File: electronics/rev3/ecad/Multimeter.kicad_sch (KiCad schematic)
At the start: 20 parts, among them J1 USB_B, SW1 GF-123-0054, U1 RP2040, U5 LM1117MP-3.3, Y1 ABLS-12.000MHZ-B4-T

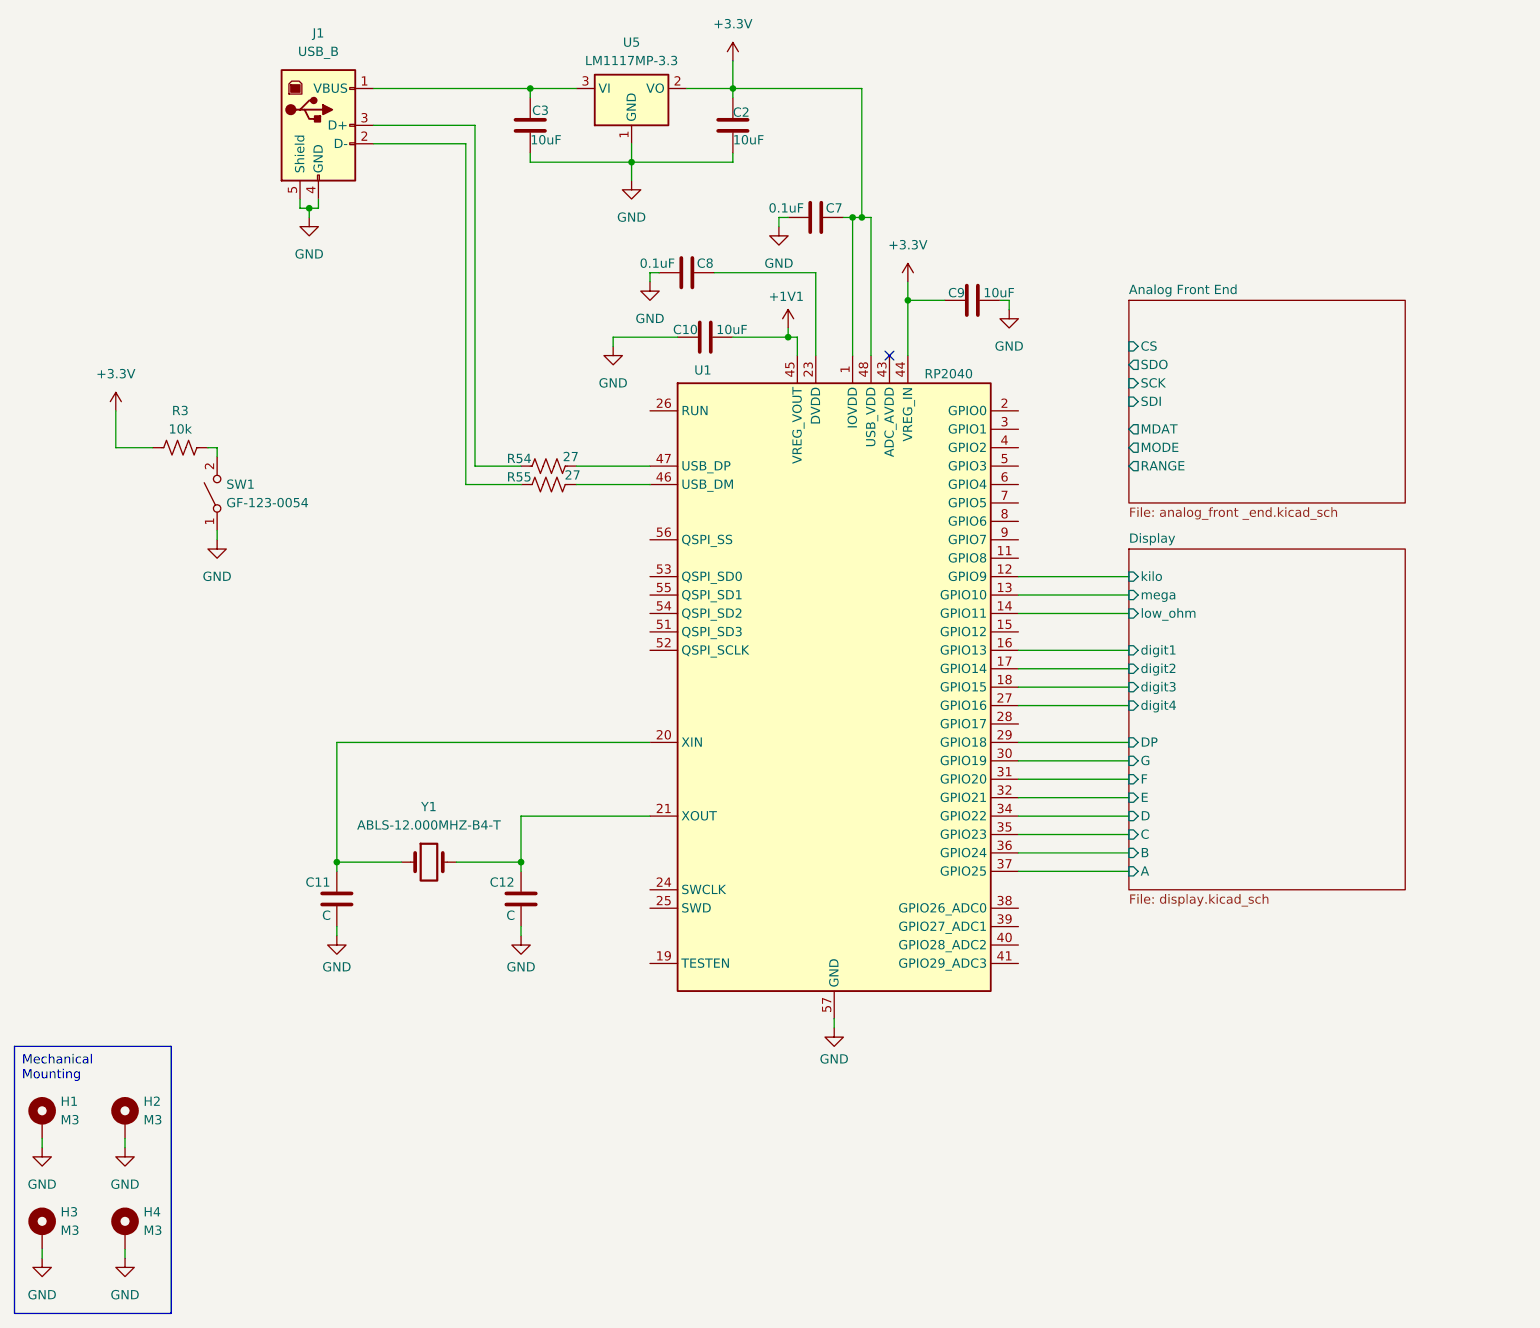
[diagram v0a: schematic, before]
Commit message: rev3 schematic work
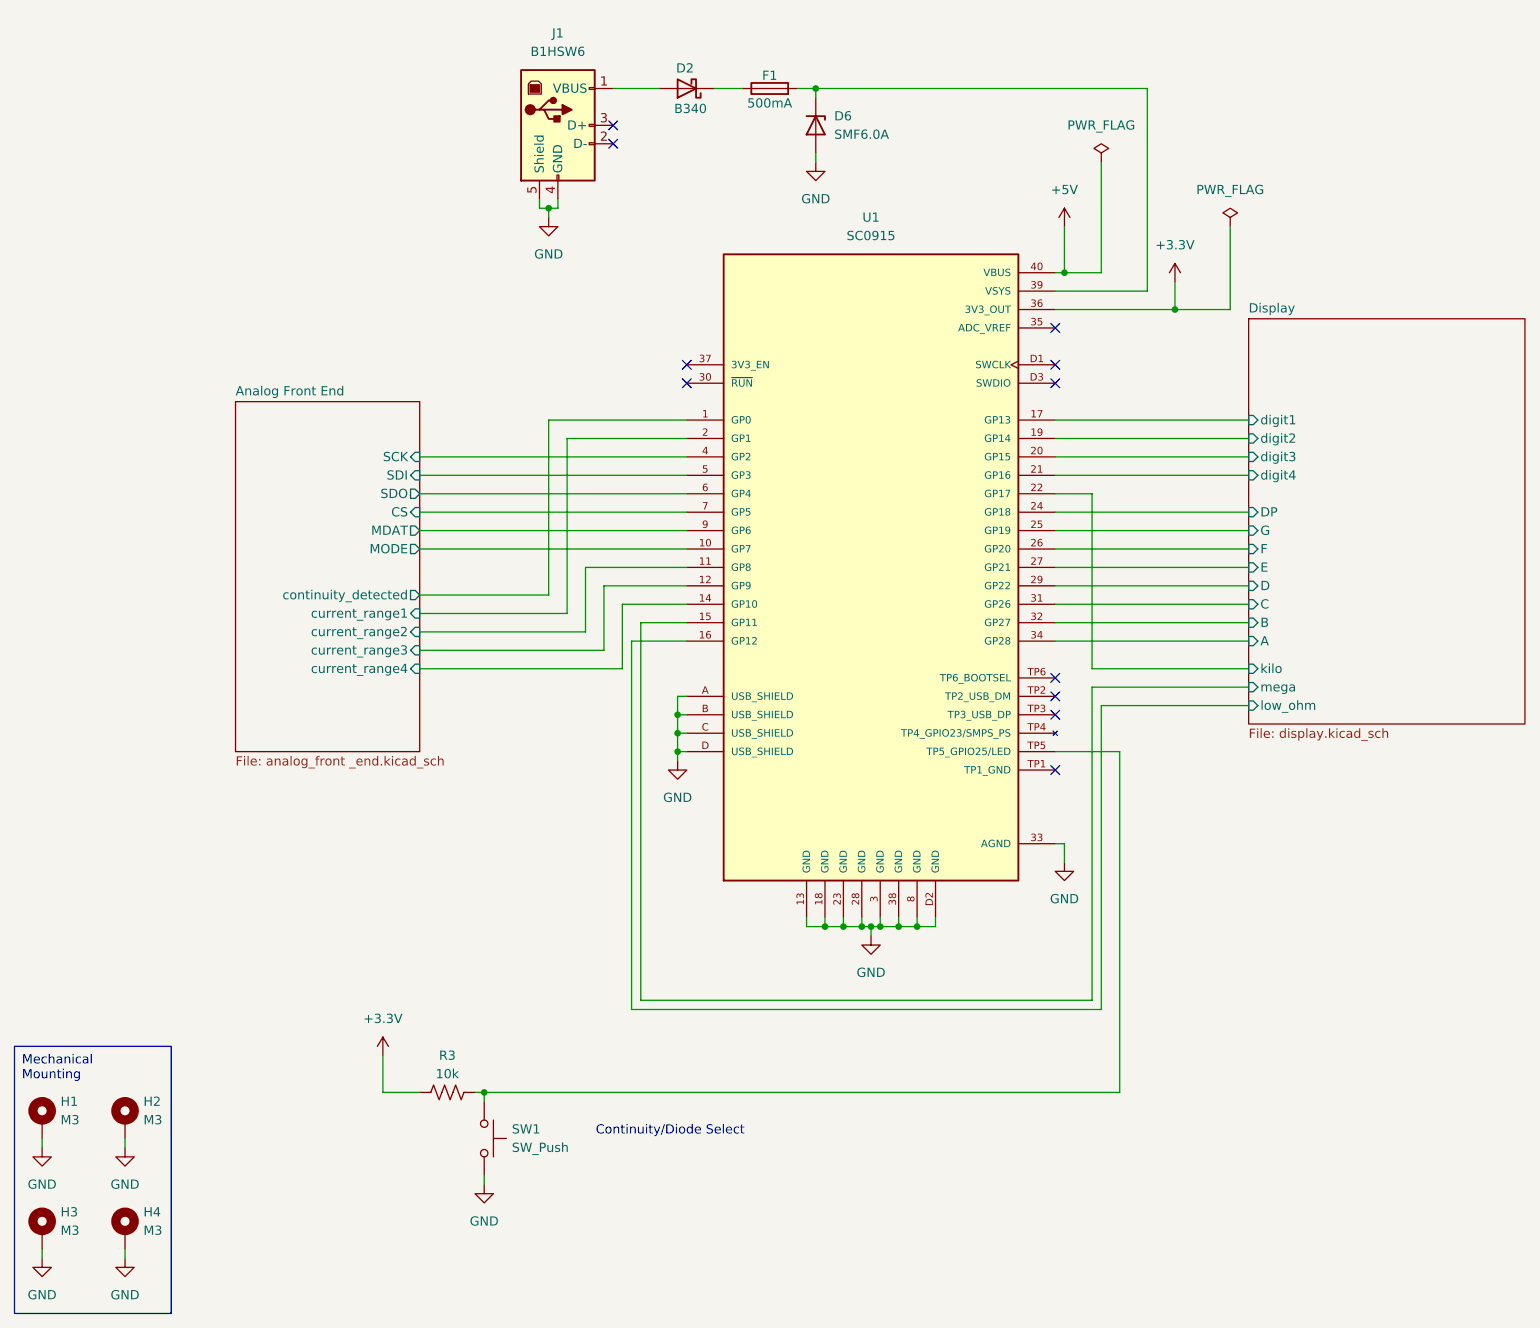
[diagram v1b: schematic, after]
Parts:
- removed C10, C2, C3, C9: 10uF, symbol Device:C
- removed C11, C12: C, symbol Device:C
- removed C7, C8: 0.1uF, symbol Device:C
- removed R54, R55: 27, symbol Device:R_US
- removed SW1: GF-123-0054, Multimeter:SW_GF-123-0054, symbol Switch:SW_SPST
- removed U1: RP2040, Package_DFN_QFN:QFN-56-1EP_7x7mm_P0.4mm_EP3.2x3.2mm, symbol MCU_RaspberryPi:RP2040
- removed U5: LM1117MP-3.3, Package_TO_SOT_SMD:SOT-223-3_TabPin2, symbol Regulator_Linear:LM1117MP-3.3
- removed Y1: ABLS-12.000MHZ-B4-T, symbol Device:Crystal
- added D2: B340, symbol Device:D_Schottky
- added D6: SMF6.0A, symbol Device:D_Zener
- added F1: 500mA, Fuse:Fuse_0805_2012Metric, symbol Device:Fuse
- added SW1: SW_Push, symbol Switch:SW_Push
- added U1: SC0915, SC0915:MODULE_SC0915, symbol multimeter_parts:SC0915
- J1: value USB_B -> B1HSW6
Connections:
- net +3.3V: now also U1.36 (3V3_OUT)
- net Analog Front End/CS: now also U1.7 (GP5)
- net Analog Front End/MDAT: now also U1.9 (GP6)
- net Analog Front End/MODE: now also U1.10 (GP7)
- net Analog Front End/SCK: now also U1.4 (GP2)
- net Analog Front End/SDI: now also U1.5 (GP3)
- net Analog Front End/SDO: now also U1.6 (GP4)
- net Display/A: now also U1.34 (GP28)
- net Display/B: now also U1.32 (GP27)
- net Display/C: now also U1.31 (GP26)
- net Display/D: now also U1.29 (GP22)
- net Display/DP: now also U1.24 (GP18)
- net Display/E: now also U1.27 (GP21)
- net Display/F: now also U1.26 (GP20)
- net Display/G: now also U1.25 (GP19)
- net Display/digit1: now also U1.17 (GP13)
- net Display/digit2: now also U1.19 (GP14)
- net Display/digit3: now also U1.20 (GP15)
- net Display/digit4: now also U1.21 (GP16)
- net Display/kilo: now also U1.22 (GP17)
- net Display/low_ohm: now also U1.16 (GP12)
- net Display/mega: now also U1.15 (GP11)
- net GND: now also D6.2 (A), SW1.2, U1.13 (GND), U1.18 (GND), U1.23 (GND), U1.28 (GND), U1.3 (GND), U1.33 (AGND), U1.38 (GND), U1.8 (GND), U1.A (USB_SHIELD), U1.B (USB_SHIELD), U1.C (USB_SHIELD), U1.D (USB_SHIELD), U1.D2 (GND)
- net at J1.1 (VBUS): now also D2.2 (A)
- net at R3.2: now also SW1.1, U1.TP5 (TP5_GPIO25/LED)
- new net: D2.1 (K), F1.1
- new net: D6.1 (K), F1.2, U1.39 (VSYS)
- new net +5V: U1.40 (VBUS)
- new net Analog Front End/continuity_detected: U1.1 (GP0)
- new net Analog Front End/current_range1: U1.2 (GP1)
- new net Analog Front End/current_range2: U1.11 (GP8)
- new net Analog Front End/current_range3: U1.12 (GP9)
- new net Analog Front End/current_range4: U1.14 (GP10)
- no-connect marks 1 -> 11
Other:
- sheet Analog Front End ports: added continuity_detected, current_range1, current_range2, current_range3, current_range4; removed RANGE
- note added: "Continuity/Diode Select"
- moved on the sheet: J1, R3

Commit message: layout work rev3
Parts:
- D2: footprint (none) -> Diode_SMD:D_SMB
- D6: footprint (none) -> Diode_SMD:D_SOD-123F
- H1, H2, H3, H4: footprint MountingHole:MountingHole_2.7mm_Pad_Via -> MountingHole:MountingHole_3.2mm_M3_Pad_Via
- J1: footprint (none) -> Connector_USB:USB_B_OST_USB-B1HSxx_Horizontal
- R3: footprint Capacitor_SMD:C_0805_2012Metric_Pad1.18x1.45mm_HandSolder -> Resistor_SMD:R_0805_2012Metric
- SW1: footprint (none) -> Button_Switch_THT:SW_PUSH_6mm
- U1: footprint SC0915:MODULE_SC0915 -> Multimeter:MODULE_SC0915
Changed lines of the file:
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@@
+	)
+	(junction
+		(at 148.59 27.94)
+		(diameter 0)
+		(color 0 0 0 0)
 	)
 	(junction
@@
 	(wire
 		(pts
-			(xy 132.08 27.94) (xy 177.8 27.94)
+			(xy 132.08 27.94) (xy 148.59 27.94)
 		)
 		(stroke
@@
 	(wire
 		(pts
+			(xy 148.59 27.94) (xy 177.8 27.94)
+		)
+		(stroke
+			(width 0)
+			(type default)
+		)
+	)
+	(wire
+		(pts
 			(xy 77.47 97.79) (xy 95.25 97.79)
 		)
@@
 		(pts
 			(xy 170.18 107.95) (xy 170.18 83.82)
+		)
+		(stroke
+			(width 0)
+			(type default)
+		)
+	)
+	(wire
+		(pts
+			(xy 148.59 25.4) (xy 148.59 27.94)
 		)
 		(stroke
@@
 			)
 		)
-		(property "Footprint" "MountingHole:MountingHole_2.7mm_Pad_Via"
+		(property "Footprint" "MountingHole:MountingHole_3.2mm_M3_Pad_Via"
 			(at 36.83 170.18 0)
 			(effects
@@
 			)
 		)
-		(property "Footprint" ""
+		(property "Footprint" "Diode_SMD:D_SMB"
 			(at 114.3 27.94 0)
 			(effects
@@
 			)
 		)
-		(property "Footprint" "MountingHole:MountingHole_2.7mm_Pad_Via"
+		(property "Footprint" "MountingHole:MountingHole_3.2mm_M3_Pad_Via"
 			(at 36.83 185.42 0)
 			(effects
@@
 			)
 		)
-		(property "Footprint" ""
+		(property "Footprint" "Diode_SMD:D_SOD-123F"
 			(at 132.08 33.02 0)
 			(effects
@@
 			)
 		)
-		(property "Footprint" "SC0915:MODULE_SC0915"
+		(property "Footprint" "Multimeter:MODULE_SC0915"
 			(at 139.7 93.98 0)
 			(effects
@@
 			)
 		)
-		(property "Footprint" "MountingHole:MountingHole_2.7mm_Pad_Via"
+		(property "Footprint" "MountingHole:MountingHole_3.2mm_M3_Pad_Via"
 			(at 25.4 170.18 0)
 			(effects
@@
 			)
 		)
-		(property "Footprint" ""
+		(property "Footprint" "Button_Switch_THT:SW_PUSH_6mm"
 			(at 91.44 172.72 0)
 			(effects
@@
 			)
 		)
-		(property "Footprint" "MountingHole:MountingHole_2.7mm_Pad_Via"
+		(property "Footprint" "MountingHole:MountingHole_3.2mm_M3_Pad_Via"
 			(at 25.4 185.42 0)
 			(effects
@@
 	)
 	(symbol
+		(lib_id "power:PWR_FLAG")
+		(at 148.59 25.4 0)
+		(unit 1)
+		(exclude_from_sim no)
+		(in_bom yes)
+		(on_board yes)
+		(dnp no)
+		(fields_autoplaced yes)
+		(property "Reference" "#FLG3"
+			(at 148.59 23.495 0)
+			(effects
+				(font
+					(size 1.27 1.27)
+				)
+				(hide yes)
+			)
+		)
+		(property "Value" "PWR_FLAG"
+			(at 148.59 20.32 0)
+			(effects
+				(font
+					(size 1.27 1.27)
+				)
+			)
+		)
+		(property "Footprint" ""
+			(at 148.59 25.4 0)
+			(effects
+				(font
+					(size 1.27 1.27)
+				)
+				(hide yes)
+			)
+		)
+		(property "Datasheet" "~"
+			(at 148.59 25.4 0)
+			(effects
+				(font
+					(size 1.27 1.27)
+				)
+				(hide yes)
+			)
+		)
+		(property "Description" "Special symbol for telling ERC where power comes from"
+			(at 148.59 25.4 0)
+			(effects
+				(font
+					(size 1.27 1.27)
+				)
+				(hide yes)
+			)
+		)
+		(pin "1"
+		)
+		(instances
+			(project ""
+				(path "/cb819000-1954-426e-958e-510a70bc03c7"
+					(reference "#FLG3")
+					(unit 1)
+				)
+			)
+		)
+	)
+	(symbol
 		(lib_id "Connector:USB_B")
 		(at 96.52 33.02 0)
@@
 			)
 		)
-		(property "Footprint" ""
+		(property "Footprint" "Connector_USB:USB_B_OST_USB-B1HSxx_Horizontal"
 			(at 100.33 34.29 0)
 			(effects
@@
 			)
 		)
-		(property "Footprint" "Capacitor_SMD:C_0805_2012Metric_Pad1.18x1.45mm_HandSolder"
+		(property "Footprint" "Resistor_SMD:R_0805_2012Metric"
 			(at 81.534 165.354 90)
 			(effects

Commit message: BOM
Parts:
- D2: Digikey Part # (none) -> B340LB-FDICT-ND; Part # (none) -> B340LB-13-F; Unit Price (none) -> 0.33
- D6: Digikey Part # (none) -> F5749CT-ND; Part # (none) -> SMF6.0A; Unit Price (none) -> 0.37
- F1: Digikey Part # (none) -> 749-MFU0805FF00500P500CT-ND; Part # (none) -> MFU0805FF00500P500; Unit Price (none) -> 0.55
- J1: Digikey Part # (none) -> ED2982-ND; Part # (none) -> USB-B1HSW6; Unit Price (none) -> 0.59
- SW1: Digikey Part # (none) -> EG5455-ND; Part # (none) -> TL1105YF160Q; Unit Price (none) -> 0.35
- U1: Digikey Part # (none) -> 2648-SC0915CT-ND; Part # (none) -> SC0915; Unit Price (none) -> 4
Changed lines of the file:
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@@
+			)
+		)
+		(property "Digikey Part #" "B340LB-FDICT-ND"
+			(at 114.3 27.94 0)
+			(effects
+				(font
+					(size 1.27 1.27)
+				)
+				(hide yes)
+			)
+		)
+		(property "Part #" "B340LB-13-F"
+			(at 114.3 27.94 0)
+			(effects
+				(font
+					(size 1.27 1.27)
+				)
+				(hide yes)
+			)
+		)
+		(property "Unit Price" "0.33"
+			(at 114.3 27.94 0)
+			(effects
+				(font
+					(size 1.27 1.27)
+				)
+				(hide yes)
 			)
 		)
@@
 			)
 		)
+		(property "Digikey Part #" "F5749CT-ND"
+			(at 132.08 33.02 0)
+			(effects
+				(font
+					(size 1.27 1.27)
+				)
+				(hide yes)
+			)
+		)
+		(property "Part #" "SMF6.0A"
+			(at 132.08 33.02 0)
+			(effects
+				(font
+					(size 1.27 1.27)
+				)
+				(hide yes)
+			)
+		)
+		(property "Unit Price" "0.37"
+			(at 132.08 33.02 0)
+			(effects
+				(font
+					(size 1.27 1.27)
+				)
+				(hide yes)
+			)
+		)
 		(pin "2"
 		)
@@
 			)
 		)
+		(property "Digikey Part #" "2648-SC0915CT-ND"
+			(at 139.7 93.98 0)
+			(effects
+				(font
+					(size 1.27 1.27)
+				)
+				(hide yes)
+			)
+		)
+		(property "Part #" "SC0915"
+			(at 139.7 93.98 0)
+			(effects
+				(font
+					(size 1.27 1.27)
+				)
+				(hide yes)
+			)
+		)
+		(property "Unit Price" "4"
+			(at 139.7 93.98 0)
+			(effects
+				(font
+					(size 1.27 1.27)
+				)
+				(hide yes)
+			)
+		)
 		(pin "3"
 		)
@@
 			)
 		)
+		(property "Digikey Part #" "EG5455-ND"
+			(at 86.36 172.72 0)
+			(effects
+				(font
+					(size 1.27 1.27)
+				)
+				(hide yes)
+			)
+		)
+		(property "Part #" "TL1105YF160Q"
+			(at 86.36 172.72 0)
+			(effects
+				(font
+					(size 1.27 1.27)
+				)
+				(hide yes)
+			)
+		)
+		(property "Unit Price" "0.35"
+			(at 86.36 172.72 0)
+			(effects
+				(font
+					(size 1.27 1.27)
+				)
+				(hide yes)
+			)
+		)
 		(pin "2"
 		)
@@
 			)
 		)
+		(property "Digikey Part #" "ED2982-ND"
+			(at 96.52 33.02 0)
+			(effects
+				(font
+					(size 1.27 1.27)
+				)
+				(hide yes)
+			)
+		)
+		(property "Part #" "USB-B1HSW6"
+			(at 96.52 33.02 0)
+			(effects
+				(font
+					(size 1.27 1.27)
+				)
+				(hide yes)
+			)
+		)
+		(property "Unit Price" "0.59"
+			(at 96.52 33.02 0)
+			(effects
+				(font
+					(size 1.27 1.27)
+				)
+				(hide yes)
+			)
+		)
 		(pin "3"
 		)
@@
 			(at 125.73 27.94 0)
 			(effects
+				(font
+					(size 1.27 1.27)
+				)
+				(hide yes)
+			)
+		)
+		(property "Digikey Part #" "749-MFU0805FF00500P500CT-ND"
+			(at 125.73 27.94 0)
+			(effects
+				(font
+					(size 1.27 1.27)
+				)
+				(hide yes)
+			)
+		)
+		(property "Part #" "MFU0805FF00500P500"
+			(at 125.73 27.94 0)
+			(effects
+				(font
+					(size 1.27 1.27)
+				)
+				(hide yes)
+			)
+		)
+		(property "Unit Price" "0.55"
+			(at 125.73 27.94 0)
+			(effects
